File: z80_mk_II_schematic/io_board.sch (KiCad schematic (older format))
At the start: 24 parts, among them J2 Conn_02x10_Odd_Even, J3 Conn_02x08_Odd_Even, J4 Conn_02x10_Odd_Even, U12 74LS00, U13 Z80_PIO, U14 74LS245, U15 74LS145, U16 74LS245, U17 Z80_CTC, U18 74LS138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

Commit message: Un-fsck something which made most of the chips into 74LS00 for some very odd reason. Also start to assign footprints.
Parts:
- D11, D12, D13, D14, D15, D16, D17, D18, D19, D20: footprint Diode_THT:D_DO-35_SOD27_P7.62mm_Horizontal -> Diodes_ThroughHole:D_DO-27_P5.08mm_Vertical_KathodeUp
- U12: footprint (none) -> Housings_DIP:DIP-14_W7.62mm_Socket
- U13, U19: footprint (none) -> Housings_DIP:DIP-40_W15.24mm
- U14, U16: footprint (none) -> Housings_DIP:DIP-20_W7.62mm_Socket
- U15, U18: footprint (none) -> Housings_DIP:DIP-16_W7.62mm_Socket
- U17: footprint (none) -> Housings_DIP:DIP-28_W15.24mm_Socket
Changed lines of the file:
@@
 F 0 "U13" H 1650 2800 50  0000 C CNN
 F 1 "Z80_PIO" H 1650 2700 50  0000 C CNN
-F 2 "" H 1650 1000 50  0001 C CNN
-F 3 "http://www.ti.com/lit/gpn/sn74ls00" H 1600 800 50  0001 C CNN
+F 2 "Housings_DIP:DIP-40_W15.24mm" H 1650 1000 50  0001 C CNN
+F 3 "" H 1600 800 50  0001 C CNN
 	1    1650 2400
 	1    0    0    -1
@@
 F 0 "U19" H 9500 2800 50  0000 C CNN
 F 1 "Z80_PIO" H 9500 2700 50  0000 C CNN
-F 2 "" H 9500 1000 50  0001 C CNN
-F 3 "http://www.ti.com/lit/gpn/sn74ls00" H 9450 800 50  0001 C CNN
+F 2 "Housings_DIP:DIP-40_W15.24mm" H 9500 1000 50  0001 C CNN
+F 3 "" H 9450 800 50  0001 C CNN
 	1    9500 2400
 	1    0    0    -1
@@
 F 0 "U17" H 5500 2800 50  0000 C CNN
 F 1 "Z80_CTC" H 5500 2700 50  0000 C CNN
-F 2 "" H 5500 1000 50  0001 C CNN
-F 3 "http://www.ti.com/lit/gpn/sn74ls00" H 5450 800 50  0001 C CNN
+F 2 "Housings_DIP:DIP-28_W15.24mm_Socket" H 5500 1000 50  0001 C CNN
+F 3 "" H 5450 800 50  0001 C CNN
 	1    5500 2400
 	1    0    0    -1
@@
 F 0 "U18" H 9300 5250 50  0000 C CNN
 F 1 "74LS138" H 9250 5150 50  0000 C CNN
-F 2 "" H 9300 5200 50  0001 C CNN
+F 2 "Housings_DIP:DIP-16_W7.62mm_Socket" H 9300 5200 50  0001 C CNN
 F 3 "" H 9300 5200 50  0001 C CNN
 	1    9300 5200
@@
 F 0 "U15" H 3250 1550 50  0000 C CNN
 F 1 "74LS145" H 3250 1450 50  0000 C CNN
-F 2 "" H 3350 1700 50  0001 C CNN
+F 2 "Housings_DIP:DIP-16_W7.62mm_Socket" H 3350 1700 50  0001 C CNN
 F 3 "" H 3350 1700 50  0001 C CNN
 	1    3350 1700
@@
 F 0 "D11" H 2950 3017 50  0000 C CNN
 F 1 "1N4148" H 2950 2926 50  0000 C CNN
-F 2 "Diode_THT:D_DO-35_SOD27_P7.62mm_Horizontal" H 2950 2625 50  0001 C CNN
+F 2 "Diodes_ThroughHole:D_DO-27_P5.08mm_Vertical_KathodeUp" H 2950 2625 50  0001 C CNN
 F 3 "https://assets.nexperia.com/documents/data-sheet/1N4148_1N4448.pdf" H 2950 2800 50  0001 C CNN
 	1    2950 2800
@@
 F 0 "D12" H 2950 3167 50  0000 C CNN
 F 1 "1N4148" H 2950 3076 50  0000 C CNN
-F 2 "Diode_THT:D_DO-35_SOD27_P7.62mm_Horizontal" H 2950 2775 50  0001 C CNN
+F 2 "Diodes_ThroughHole:D_DO-27_P5.08mm_Vertical_KathodeUp" H 2950 2775 50  0001 C CNN
 F 3 "https://assets.nexperia.com/documents/data-sheet/1N4148_1N4448.pdf" H 2950 2950 50  0001 C CNN
 	1    2950 2950
@@
 F 0 "D13" H 2950 3317 50  0000 C CNN
 F 1 "1N4148" H 2950 3226 50  0000 C CNN
-F 2 "Diode_THT:D_DO-35_SOD27_P7.62mm_Horizontal" H 2950 2925 50  0001 C CNN
+F 2 "Diodes_ThroughHole:D_DO-27_P5.08mm_Vertical_KathodeUp" H 2950 2925 50  0001 C CNN
 F 3 "https://assets.nexperia.com/documents/data-sheet/1N4148_1N4448.pdf" H 2950 3100 50  0001 C CNN
 	1    2950 3100
@@
 F 0 "D14" H 2950 3467 50  0000 C CNN
 F 1 "1N4148" H 2950 3376 50  0000 C CNN
-F 2 "Diode_THT:D_DO-35_SOD27_P7.62mm_Horizontal" H 2950 3075 50  0001 C CNN
+F 2 "Diodes_ThroughHole:D_DO-27_P5.08mm_Vertical_KathodeUp" H 2950 3075 50  0001 C CNN
 F 3 "https://assets.nexperia.com/documents/data-sheet/1N4148_1N4448.pdf" H 2950 3250 50  0001 C CNN
 	1    2950 3250
@@
 F 0 "D15" H 2950 3617 50  0000 C CNN
 F 1 "1N4148" H 2950 3526 50  0000 C CNN
-F 2 "Diode_THT:D_DO-35_SOD27_P7.62mm_Horizontal" H 2950 3225 50  0001 C CNN
+F 2 "Diodes_ThroughHole:D_DO-27_P5.08mm_Vertical_KathodeUp" H 2950 3225 50  0001 C CNN
 F 3 "https://assets.nexperia.com/documents/data-sheet/1N4148_1N4448.pdf" H 2950 3400 50  0001 C CNN
 	1    2950 3400
@@
 F 0 "D16" H 2950 3767 50  0000 C CNN
 F 1 "1N4148" H 2950 3676 50  0000 C CNN
-F 2 "Diode_THT:D_DO-35_SOD27_P7.62mm_Horizontal" H 2950 3375 50  0001 C CNN
+F 2 "Diodes_ThroughHole:D_DO-27_P5.08mm_Vertical_KathodeUp" H 2950 3375 50  0001 C CNN
 F 3 "https://assets.nexperia.com/documents/data-sheet/1N4148_1N4448.pdf" H 2950 3550 50  0001 C CNN
 	1    2950 3550
@@
 F 0 "D17" H 2950 3917 50  0000 C CNN
 F 1 "1N4148" H 2950 3826 50  0000 C CNN
-F 2 "Diode_THT:D_DO-35_SOD27_P7.62mm_Horizontal" H 2950 3525 50  0001 C CNN
+F 2 "Diodes_ThroughHole:D_DO-27_P5.08mm_Vertical_KathodeUp" H 2950 3525 50  0001 C CNN
 F 3 "https://assets.nexperia.com/documents/data-sheet/1N4148_1N4448.pdf" H 2950 3700 50  0001 C CNN
 	1    2950 3700
@@
 F 0 "D18" H 2950 4067 50  0000 C CNN
 F 1 "1N4148" H 2950 3976 50  0000 C CNN
-F 2 "Diode_THT:D_DO-35_SOD27_P7.62mm_Horizontal" H 2950 3675 50  0001 C CNN
+F 2 "Diodes_ThroughHole:D_DO-27_P5.08mm_Vertical_KathodeUp" H 2950 3675 50  0001 C CNN
 F 3 "https://assets.nexperia.com/documents/data-sheet/1N4148_1N4448.pdf" H 2950 3850 50  0001 C CNN
 	1    2950 3850
@@
 F 0 "D19" H 2950 4217 50  0000 C CNN
 F 1 "1N4148" H 2950 4126 50  0000 C CNN
-F 2 "Diode_THT:D_DO-35_SOD27_P7.62mm_Horizontal" H 2950 3825 50  0001 C CNN
+F 2 "Diodes_ThroughHole:D_DO-27_P5.08mm_Vertical_KathodeUp" H 2950 3825 50  0001 C CNN
 F 3 "https://assets.nexperia.com/documents/data-sheet/1N4148_1N4448.pdf" H 2950 4000 50  0001 C CNN
 	1    2950 4000
@@
 F 0 "D20" H 2950 4367 50  0000 C CNN
 F 1 "1N4148" H 2950 4276 50  0000 C CNN
-F 2 "Diode_THT:D_DO-35_SOD27_P7.62mm_Horizontal" H 2950 3975 50  0001 C CNN
+F 2 "Diodes_ThroughHole:D_DO-27_P5.08mm_Vertical_KathodeUp" H 2950 3975 50  0001 C CNN
 F 3 "https://assets.nexperia.com/documents/data-sheet/1N4148_1N4448.pdf" H 2950 4150 50  0001 C CNN
 	1    2950 4150
@@
 F 0 "U14" H 2100 7000 50  0000 C CNN
 F 1 "74LS245" H 2100 6450 50  0000 C CNN
-F 2 "" H 2100 6750 50  0001 C CNN
+F 2 "Housings_DIP:DIP-20_W7.62mm_Socket" H 2100 6750 50  0001 C CNN
 F 3 "" H 2100 6750 50  0001 C CNN
 	1    2100 6750
@@
 F 0 "U16" H 3750 7000 50  0000 C CNN
 F 1 "74LS245" H 3750 6450 50  0000 C CNN
-F 2 "" H 3750 6750 50  0001 C CNN
+F 2 "Housings_DIP:DIP-20_W7.62mm_Socket" H 3750 6750 50  0001 C CNN
 F 3 "" H 3750 6750 50  0001 C CNN
 	1    3750 6750
@@
 F 0 "U12" V 1400 4600 50  0000 C CNN
 F 1 "74LS00" V 1700 4650 50  0000 L CNN
-F 2 "" H 1450 4600 50  0001 C CNN
+F 2 "Housings_DIP:DIP-14_W7.62mm_Socket" H 1450 4600 50  0001 C CNN
 F 3 "http://www.ti.com/lit/gpn/sn74ls00" H 1450 4600 50  0001 C CNN
 	3    1450 4600
@@
 F 0 "U12" V 1800 4600 50  0000 C CNN
 F 1 "74LS00" V 1895 4788 50  0001 L CNN
-F 2 "" H 1850 4600 50  0001 C CNN
+F 2 "Housings_DIP:DIP-14_W7.62mm_Socket" H 1850 4600 50  0001 C CNN
 F 3 "http://www.ti.com/lit/gpn/sn74ls00" H 1850 4600 50  0001 C CNN
 	4    1850 4600
@@
 F 0 "U12" V 1600 5300 50  0000 C CNN
 F 1 "74LS00" V 1695 5488 50  0001 L CNN
-F 2 "" H 1650 5300 50  0001 C CNN
+F 2 "Housings_DIP:DIP-14_W7.62mm_Socket" H 1650 5300 50  0001 C CNN
 F 3 "http://www.ti.com/lit/gpn/sn74ls00" H 1650 5300 50  0001 C CNN
 	2    1650 5300
@@
 F 0 "U12" H 5300 7000 50  0000 L CNN
 F 1 "74LS00" H 5250 6900 50  0000 L CNN
-F 2 "" H 5400 6950 50  0001 C CNN
+F 2 "Housings_DIP:DIP-14_W7.62mm_Socket" H 5400 6950 50  0001 C CNN
 F 3 "http://www.ti.com/lit/gpn/sn74ls00" H 5400 6950 50  0001 C CNN
 	5    5400 6950

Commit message: Add some no-connection symbols.
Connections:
- net GND: now also U15.8 (GND)
- no-connect marks 0 -> 32
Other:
- note added: "The unused pins here\nshould be connected to GND\nand +5V as per beeb user\nport."
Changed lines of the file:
@@
 	1    0    0    -1
 $EndComp
+NoConn ~ 10000 2500
+NoConn ~ 10000 2600
+NoConn ~ 10000 2700
+NoConn ~ 10000 2800
+NoConn ~ 10000 2900
+NoConn ~ 10000 3000
+NoConn ~ 10000 3100
+NoConn ~ 10000 3200
+NoConn ~ 10000 3400
+NoConn ~ 10000 3500
+NoConn ~ 2150 3400
+NoConn ~ 2150 3500
+NoConn ~ 2150 2200
+NoConn ~ 2150 2300
+$Comp
+L power:GND #PWR0114
+U 1 1 5FD8B7DA
+P 3350 2500
+F 0 "#PWR0114" H 3350 2250 50  0001 C CNN
+F 1 "GND" H 3355 2327 50  0000 C CNN
+F 2 "" H 3350 2500 50  0001 C CNN
+F 3 "" H 3350 2500 50  0001 C CNN
+	1    3350 2500
+	1    0    0    -1
+$EndComp
+NoConn ~ 2150 1800
+NoConn ~ 2150 1900
+NoConn ~ 2150 2000
+NoConn ~ 6000 2550
+NoConn ~ 6000 2650
+NoConn ~ 6000 2850
+NoConn ~ 10050 3700
+NoConn ~ 10050 3800
+NoConn ~ 10050 3900
+NoConn ~ 10050 4000
+NoConn ~ 10050 4100
+NoConn ~ 10050 4200
+NoConn ~ 10050 4300
+NoConn ~ 10050 4400
+NoConn ~ 10050 4500
+Text Notes 8850 4300 0    50   ~ 0
+The unused pins here\nshould be connected to GND\nand +5V as per beeb user\nport.
+NoConn ~ 9800 5400
+NoConn ~ 9800 5500
+NoConn ~ 9800 5600
 Wire Bus Line
 	6700 850  6700 4700

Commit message: Add some missing gates and wiring.
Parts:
- added unit 1 of U12
- added U20: 74LS04, Housings_DIP:DIP-14_W7.62mm, symbol 74xx:74LS04
- added U26: 74LS00, Housings_DIP:DIP-14_W7.62mm, symbol 74xx:74LS00
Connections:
- net ~M1~: now also U26.1; no longer U13.37 (~M1~)
- net ~RESET~: now also U26.2
- net ~WR~: now also U20.13; no longer J3.12 (Pin_12)
- net ~RAM_WR_EN~: now reaches U13.7 (PA7)
- new net: U20.11, U20.12
- new net: U26.3, U26.4, U26.5
- new net ~M1_PIO~: U13.37 (~M1~), U26.6
- new net ~WRB~: J3.12 (Pin_12), U20.10
- no-connect marks 32 -> 33
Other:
- note added: "Not sure why ~WR~ was\nbuffered like this."
- note added: "PIO reset-via-M1 CCT - see data sheet"
- note added: "Should probably\nbe connected to\n~M1_PIO~"
- note added: "Unused inputs currently floating.\nShould be connected to 0V or +5V"
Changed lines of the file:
@@
 	1150 2700 1050 2700
 Wire Wire Line
-	1150 2600 1050 2600
-Wire Wire Line
 	1150 2500 800  2500
-Text HLabel 1050 2600 0    50   Input ~ 0
-~M1~
 Text HLabel 1050 2700 0    50   Input ~ 0
 ~IORQ~
@@
 	7200 2500 7350 2500
 Wire Wire Line
-	7850 2300 8200 2300
-Text HLabel 8200 2300 2    50   Input ~ 0
-~WR~
+	7850 2300 8150 2300
 $Comp
 L Connector_Generic:Conn_02x10_Odd_Even J4
@@
 ~RD~
 Wire Wire Line
-	7200 5150 7050 5150
-Text HLabel 7050 5150 0    50   Input ~ 0
-~WR~
-Wire Wire Line
 	6700 5350 7100 5350
 Wire Wire Line
@@
 NoConn ~ 2150 1800
 NoConn ~ 2150 1900
-NoConn ~ 2150 2000
 NoConn ~ 6000 2550
 NoConn ~ 6000 2650
@@
 NoConn ~ 10050 4400
 NoConn ~ 10050 4500
-Text Notes 8850 4300 0    50   ~ 0
+Text Notes 9850 4300 2    50   ~ 0
 The unused pins here\nshould be connected to GND\nand +5V as per beeb user\nport.
 NoConn ~ 9800 5400
 NoConn ~ 9800 5500
 NoConn ~ 9800 5600
+NoConn ~ 800  4450
+NoConn ~ 1000 4450
+Text Notes 950  5600 1    40   ~ 0
+Unused inputs currently floating.\nShould be connected to 0V or +5V
+$Comp
+L 74xx:74LS00 U12
+U 1 1 5FA376B0
+P 900 4150
+F 0 "U12" H 900 4150 50  0000 C CNN
+F 1 "74LS00" V 945 4338 50  0001 L CNN
+F 2 "Housings_DIP:DIP-14_W7.62mm_Socket" H 900 4150 50  0001 C CNN
+F 3 "http://www.ti.com/lit/gpn/sn74ls00" H 900 4150 50  0001 C CNN
+	1    900  4150
+	0    -1   -1   0
+$EndComp
+Text Label 7900 2300 0    50   ~ 0
+~WRB~
+$Comp
+L 74xx:74LS04 U?
+U 5 1 5FB7DC06
+P 10450 6250
+AR Path="/5F996112/6026683D/5FB7DC06" Ref="U?"  Part="3"
+AR Path="/5F996112/6029665D/5FB7DC06" Ref="U?"  Part="4"
+AR Path="/5F996112/5FB7DC06" Ref="U20"  Part="5"
+F 0 "U20" H 10400 6250 50  0000 C CNN
+F 1 "74LS04" H 10450 6050 50  0000 C CNN
+F 2 "Housings_DIP:DIP-14_W7.62mm" H 10450 6250 50  0001 C CNN
+F 3 "http://www.ti.com/lit/gpn/sn74LS04" H 10450 6250 50  0001 C CNN
+	5    10450 6250
+	1    0    0    -1
+$EndComp
+$Comp
+L 74xx:74LS04 U?
+U 6 1 5FBA2C4C
+P 9750 6250
+AR Path="/5F996112/6026683D/5FBA2C4C" Ref="U?"  Part="3"
+AR Path="/5F996112/6029665D/5FBA2C4C" Ref="U?"  Part="4"
+AR Path="/5F996112/5FBA2C4C" Ref="U20"  Part="6"
+F 0 "U20" H 9700 6250 50  0000 C CNN
+F 1 "74LS04" H 9750 6050 50  0000 C CNN
+F 2 "Housings_DIP:DIP-14_W7.62mm" H 9750 6250 50  0001 C CNN
+F 3 "http://www.ti.com/lit/gpn/sn74LS04" H 9750 6250 50  0001 C CNN
+	6    9750 6250
+	1    0    0    -1
+$EndComp
+Wire Wire Line
+	10050 6250 10150 6250
+Wire Wire Line
+	10750 6250 11000 6250
+Text Label 10800 6250 0    50   ~ 0
+~WRB~
+Wire Wire Line
+	7200 5150 7050 5150
+Wire Wire Line
+	7050 5150 7050 5200
+Wire Wire Line
+	7050 5200 6700 5200
+Text Label 6700 5200 0    50   ~ 0
+~WRB~
+Wire Wire Line
+	9450 6250 9250 6250
+Text HLabel 9250 6250 0    50   Input ~ 0
+~WR~
+Text Notes 9700 6050 0    40   ~ 0
+Not sure why ~WR~ was\nbuffered like this.
+$Comp
+L 74xx:74LS00 U?
+U 1 1 5FE03CE8
+P 6950 6150
+AR Path="/5F996112/6026683D/5FE03CE8" Ref="U?"  Part="1"
+AR Path="/5F996112/5FE03CE8" Ref="U26"  Part="1"
+F 0 "U26" V 6950 6250 50  0000 R CNN
+F 1 "74LS00" H 7050 5900 50  0000 R CNN
+F 2 "Housings_DIP:DIP-14_W7.62mm" H 6950 6150 50  0001 C CNN
+F 3 "http://www.ti.com/lit/gpn/sn74ls00" H 6950 6150 50  0001 C CNN
+	1    6950 6150
+	1    0    0    -1
+$EndComp
+$Comp
+L 74xx:74LS00 U?
+U 2 1 5FE03CEE
+P 7700 6150
+AR Path="/5F996112/6026683D/5FE03CEE" Ref="U?"  Part="2"
+AR Path="/5F996112/5FE03CEE" Ref="U26"  Part="2"
+F 0 "U26" V 7700 6250 50  0000 R CNN
+F 1 "74LS00" H 7800 5900 50  0000 R CNN
+F 2 "Housings_DIP:DIP-14_W7.62mm" H 7700 6150 50  0001 C CNN
+F 3 "http://www.ti.com/lit/gpn/sn74ls00" H 7700 6150 50  0001 C CNN
+	2    7700 6150
+	1    0    0    -1
+$EndComp
+Wire Wire Line
+	7400 6050 7350 6050
+Wire Wire Line
+	7350 6050 7350 6150
+Wire Wire Line
+	7350 6250 7400 6250
+Wire Wire Line
+	7250 6150 7350 6150
+Connection ~ 7350 6150
+Wire Wire Line
+	7350 6150 7350 6250
+Wire Wire Line
+	6650 6050 6450 6050
+Wire Wire Line
+	6650 6250 6450 6250
+Text HLabel 6450 6050 0    50   Input ~ 0
+~M1~
+Text HLabel 6450 6250 0    50   Input ~ 0
+~RESET~
+Wire Wire Line
+	8000 6150 8350 6150
+Text Label 8050 6150 0    50   ~ 0
+~M1_PIO~
+Wire Wire Line
+	800  2600 1150 2600
+Text Label 800  2600 0    50   ~ 0
+~M1_PIO~
+Wire Wire Line
+	2150 2000 2300 2000
+Text HLabel 2400 1050 2    50   Output ~ 0
+~RAM_WR_EN~
+Wire Wire Line
+	2300 2000 2300 1050
+Wire Wire Line
+	2300 1050 2400 1050
+Text Notes 6650 5950 0    40   ~ 0
+PIO reset-via-M1 CCT - see data sheet
+Text Notes 7800 3100 0    40   ~ 0
+Should probably\nbe connected to\n~M1_PIO~
+Wire Notes Line
+	8350 2950 8450 2950
+Wire Notes Line
+	8450 2950 8450 2600
+Wire Notes Line
+	8450 2600 8650 2600
 Wire Bus Line
 	6700 850  6700 4700
@@
 	6900 650  6900 4500
 Wire Bus Line
+	1300 6350 1300 7350
+Wire Bus Line
+	2950 6350 2950 7350
+Wire Bus Line
+	4500 6350 4500 7600
+Wire Bus Line
 	2850 5900 2850 6850
 Wire Bus Line
@@
 	4650 650  4650 1900
 Wire Bus Line
-	4500 6350 4500 7600
-Wire Bus Line
-	2950 6350 2950 7350
-Wire Bus Line
-	1300 6350 1300 7350
-Wire Bus Line
 	700  650  700  5700

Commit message: Complete RAM_WR_EN wiring.
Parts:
- added R?: 10K, symbol Device:R_Small
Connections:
- net +5V: now also R?.1
- net ~IORQ~: now also R?.2
- net ~RAM_WR_EN~ renamed RAM_WR_EN
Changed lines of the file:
@@
 	2150 2000 2300 2000
 Text HLabel 2400 1050 2    50   Output ~ 0
-~RAM_WR_EN~
+RAM_WR_EN
 Wire Wire Line
 	2300 2000 2300 1050
@@
 Wire Notes Line
 	8450 2600 8650 2600
+$Comp
+L power:+5V #PWR?
+U 1 1 5FA41785
+P 4900 6450
+F 0 "#PWR?" H 4900 6300 50  0001 C CNN
+F 1 "+5V" H 4915 6623 50  0000 C CNN
+F 2 "" H 4900 6450 50  0001 C CNN
+F 3 "" H 4900 6450 50  0001 C CNN
+	1    4900 6450
+	-1   0    0    -1
+$EndComp
+Text HLabel 4900 6900 3    50   Input ~ 0
+~IORQ~
+$Comp
+L Device:R_Small R?
+U 1 1 5FA439DA
+P 4900 6650
+F 0 "R?" H 4959 6696 50  0000 L CNN
+F 1 "10K" H 4959 6605 50  0000 L CNN
+F 2 "" H 4900 6650 50  0001 C CNN
+F 3 "~" H 4900 6650 50  0001 C CNN
+	1    4900 6650
+	1    0    0    -1
+$EndComp
+Wire Wire Line
+	4900 6750 4900 6900
+Wire Wire Line
+	4900 6550 4900 6450
 Wire Bus Line
 	6700 850  6700 4700

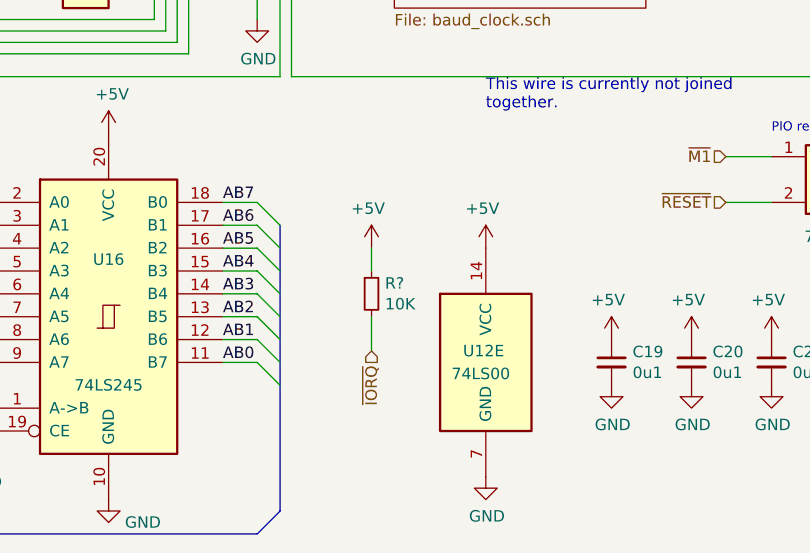
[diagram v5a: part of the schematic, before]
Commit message: Add pull-up for /IORQ on IO board.
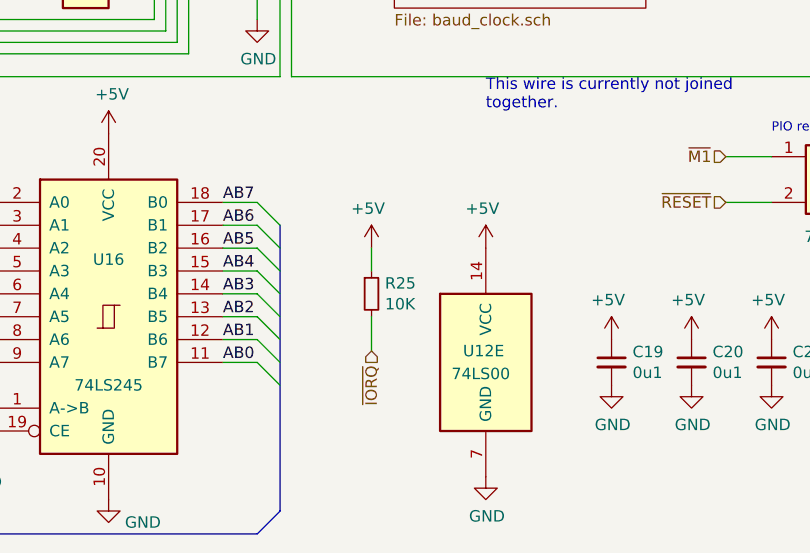
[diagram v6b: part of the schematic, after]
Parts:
- gave numbers to parts that had none: 1
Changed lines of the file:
@@
 	8450 2600 8650 2600
 $Comp
-L power:+5V #PWR?
+L power:+5V #PWR0119
 U 1 1 5FA41785
 P 4900 6450
-F 0 "#PWR?" H 4900 6300 50  0001 C CNN
+F 0 "#PWR0119" H 4900 6300 50  0001 C CNN
 F 1 "+5V" H 4915 6623 50  0000 C CNN
 F 2 "" H 4900 6450 50  0001 C CNN
@@
 ~IORQ~
 $Comp
-L Device:R_Small R?
+L Device:R_Small R25
 U 1 1 5FA439DA
 P 4900 6650
-F 0 "R?" H 4959 6696 50  0000 L CNN
+F 0 "R25" H 4959 6696 50  0000 L CNN
 F 1 "10K" H 4959 6605 50  0000 L CNN
 F 2 "" H 4900 6650 50  0001 C CNN
